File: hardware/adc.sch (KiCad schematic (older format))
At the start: 39 parts, among them U39 LP5907-3.0, U8 LTC2292

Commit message: Finished design, began routing.
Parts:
- U10: renamed from U39; value LP5907-3.0 -> LP5907MFX-3.0
- renumbered C25 to C100, C225 to C101, C248 to C75, C31 to C76, C249 to C77, C163 to C78, C164 to C79, C165 to C80, C166 to C81, C167 to C82, C168 to C83, C222 to C84, C230 to C85, C231 to C86, C217 to C87, C218 to C88, C19 to C89, C20 to C90, C223 to C91, C216 to C92, C220 to C93, C22 to C94, C224 to C95, C221 to C96, C23 to C97, C24 to C98, C27 to C99, FB16 to FB5, R97 to R28, R98 to R29, R99 to R30, R100 to R31, R91 to R32, R92 to R33, R93 to R34, R20 to R35, R21 to R36, U8 to U11

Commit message: Completed clock placement and routing.
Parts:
- removed C86: 100n, Capacitor_SMD:C_0402_1005Metric, symbol Device:C
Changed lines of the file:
@@
 	0    1    1    0
 $EndComp
-Wire Wire Line
-	4900 1050 5050 1050
-$Comp
-L Device:C C86
-U 1 1 5D84B592
-P 5050 1250
-F 0 "C86" H 5165 1296 50  0000 L CNN
-F 1 "100n" H 5165 1205 50  0000 L CNN
-F 2 "Capacitor_SMD:C_0402_1005Metric" H 5088 1100 30  0001 C CNN
-F 3 "" H 5050 1250 60  0000 C CNN
-F 4 "CL05B104KO5NNNC" H -550 50  50  0001 C CNN "MFN"
-	1    5050 1250
-	1    0    0    -1
-$EndComp
-Wire Wire Line
-	5050 1100 5050 1050
-Connection ~ 5050 1050
-Wire Wire Line
-	5050 1050 5400 1050
-$Comp
-L power:GND #PWR079
-U 1 1 5D852C8A
-P 5050 1450
-F 0 "#PWR079" H 5050 1200 50  0001 C CNN
-F 1 "GND" H 5055 1277 50  0000 C CNN
-F 2 "" H 5050 1450 50  0001 C CNN
-F 3 "" H 5050 1450 50  0001 C CNN
-	1    5050 1450
-	1    0    0    -1
-$EndComp
-Wire Wire Line
-	5050 1450 5050 1400
-$Comp
-L Device:C C85
-U 1 1 5D85A49D
-P 4450 1250
-F 0 "C85" H 4565 1296 50  0000 L CNN
-F 1 "100n" H 4565 1205 50  0000 L CNN
-F 2 "Capacitor_SMD:C_0402_1005Metric" H 4488 1100 30  0001 C CNN
-F 3 "" H 4450 1250 60  0000 C CNN
-F 4 "CL05B104KO5NNNC" H -1150 50  50  0001 C CNN "MFN"
-	1    4450 1250
-	1    0    0    -1
-$EndComp
-Wire Wire Line
-	4450 1100 4450 1050
-Connection ~ 4450 1050
-Wire Wire Line
-	4450 1050 4600 1050
-$Comp
-L power:GND #PWR078
-U 1 1 5D861E18
-P 4450 1450
-F 0 "#PWR078" H 4450 1200 50  0001 C CNN
-F 1 "GND" H 4455 1277 50  0000 C CNN
-F 2 "" H 4450 1450 50  0001 C CNN
-F 3 "" H 4450 1450 50  0001 C CNN
-	1    4450 1450
-	1    0    0    -1
-$EndComp
-Wire Wire Line
-	4450 1450 4450 1400
 Connection ~ 4000 1050
-Wire Wire Line
-	4000 1050 4450 1050
 Wire Wire Line
 	3700 1050 4000 1050
@@
 	0    1    1    0
 $EndComp
+Wire Wire Line
+	4900 1050 5400 1050
+Wire Wire Line
+	4000 1050 4450 1050
+Wire Wire Line
+	4450 1050 4600 1050
+Connection ~ 4450 1050
+Wire Wire Line
+	4450 1100 4450 1050
+Wire Wire Line
+	4450 1450 4450 1400
+$Comp
+L power:GND #PWR078
+U 1 1 5D861E18
+P 4450 1450
+F 0 "#PWR078" H 4450 1200 50  0001 C CNN
+F 1 "GND" H 4455 1277 50  0000 C CNN
+F 2 "" H 4450 1450 50  0001 C CNN
+F 3 "" H 4450 1450 50  0001 C CNN
+	1    4450 1450
+	1    0    0    -1
+$EndComp
+$Comp
+L Device:C C85
+U 1 1 5D85A49D
+P 4450 1250
+F 0 "C85" H 4565 1296 50  0000 L CNN
+F 1 "100n" H 4565 1205 50  0000 L CNN
+F 2 "Capacitor_SMD:C_0402_1005Metric" H 4488 1100 30  0001 C CNN
+F 3 "" H 4450 1250 60  0000 C CNN
+F 4 "CL05B104KO5NNNC" H -1150 50  50  0001 C CNN "MFN"
+	1    4450 1250
+	1    0    0    -1
+$EndComp
 $EndSCHEMATC

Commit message: Place/route for ft2232h.
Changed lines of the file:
@@
 F 3 "" H 5050 3650 60  0000 C CNN
 	1    5050 3650
-	1    0    0    -1
+	-1   0    0    -1
 $EndComp
 Text HLabel 8200 2650 2    60   Output ~ 0

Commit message: Better MFNs for RF DC blocking caps.
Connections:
- net AINA+: now reaches C78.2, C79.1, R28.1, U11.1 (AINA+)
- net AINB-: now reaches C82.2, C83.1, R31.1, U11.15 (AINB-)
- net AINB+: now reaches C81.2, C82.1, R29.1, U11.16 (AINB+)
- net AINA-: now reaches C79.2, C80.1, R30.1, U11.2 (AINA-)
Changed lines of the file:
@@
 	1    0    0    -1
 $EndComp
+Text Label 5550 3050 0    50   ~ 0
+AINA+
+Text Label 5550 3150 0    50   ~ 0
+AINA-
+Text Label 5550 4450 0    50   ~ 0
+AINB+
+Text Label 5550 4550 0    50   ~ 0
+AINB-
 $EndSCHEMATC

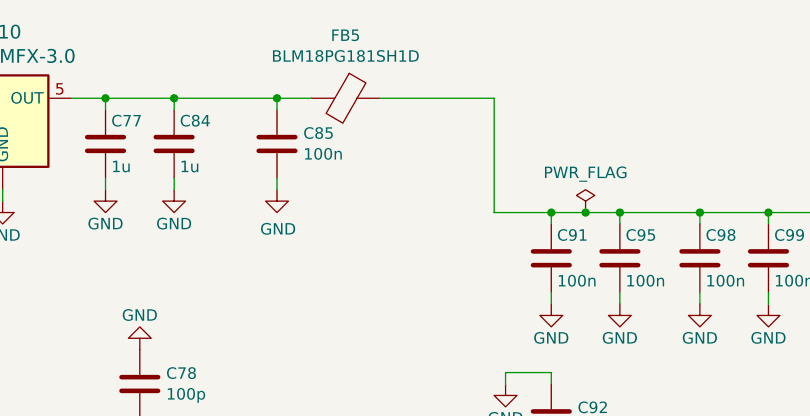
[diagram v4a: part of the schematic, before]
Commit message: Completed receivers.
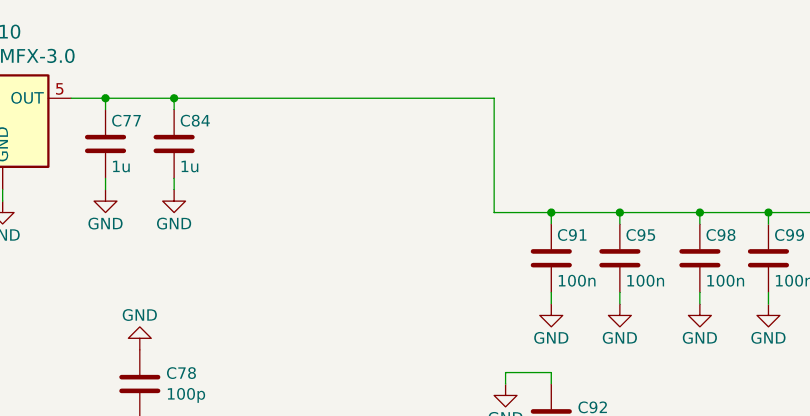
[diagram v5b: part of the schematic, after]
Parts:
- removed C85: 100n, Capacitor_SMD:C_0402_1005Metric, symbol Device:C
- removed FB5: BLM18PG181SH1D, Inductor_SMD:L_0603_1608Metric, symbol Device:Ferrite_Bead
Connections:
- net at C91.1, C95.1, C98.1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: now also C77.1, C84.1, U10.5 (OUT)
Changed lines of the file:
@@
 Wire Wire Line
 	3250 1500 3250 1450
-$Comp
-L Device:Ferrite_Bead FB?
-U 1 1 5D83CEED
-P 4750 1050
-AR Path="/5D83CEED" Ref="FB?"  Part="1"
-AR Path="/59395D6A/583E250D/5D83CEED" Ref="FB5"  Part="1"
-F 0 "FB5" V 4476 1050 50  0000 C CNN
-F 1 "BLM18PG181SH1D" V 4567 1050 50  0000 C CNN
-F 2 "Inductor_SMD:L_0603_1608Metric" H 4750 1050 60  0001 C CNN
-F 3 "https://www.murata.com/en-us/products/productdata/8796738650142/ENFA0003.pdf" H 4750 1050 60  0001 C CNN
-F 4 "BLM18PG181SH1D" H 400 -4250 50  0001 C CNN "MFN"
-	1    4750 1050
-	0    1    1    0
-$EndComp
 Connection ~ 4000 1050
 Wire Wire Line
@@
 	5650 1600 5650 1550
 Connection ~ 5650 1550
-Wire Wire Line
-	5650 1550 5800 1550
-$Comp
-L power:PWR_FLAG #FLG05
-U 1 1 5C415896
-P 5800 1550
-F 0 "#FLG05" H 5800 1625 50  0001 C CNN
-F 1 "PWR_FLAG" H 5800 1724 50  0000 C CNN
-F 2 "" H 5800 1550 50  0001 C CNN
-F 3 "~" H 5800 1550 50  0001 C CNN
-	1    5800 1550
-	1    0    0    -1
-$EndComp
-Connection ~ 5800 1550
-Wire Wire Line
-	5800 1550 5950 1550
 Wire Wire Line
 	5400 1550 5650 1550
@@
 	0    1    1    0
 $EndComp
-Wire Wire Line
-	4900 1050 5400 1050
-Wire Wire Line
-	4000 1050 4450 1050
-Wire Wire Line
-	4450 1050 4600 1050
-Connection ~ 4450 1050
-Wire Wire Line
-	4450 1100 4450 1050
-Wire Wire Line
-	4450 1450 4450 1400
-$Comp
-L power:GND #PWR078
-U 1 1 5D861E18
-P 4450 1450
-F 0 "#PWR078" H 4450 1200 50  0001 C CNN
-F 1 "GND" H 4455 1277 50  0000 C CNN
-F 2 "" H 4450 1450 50  0001 C CNN
-F 3 "" H 4450 1450 50  0001 C CNN
-	1    4450 1450
-	1    0    0    -1
-$EndComp
-$Comp
-L Device:C C85
-U 1 1 5D85A49D
-P 4450 1250
-F 0 "C85" H 4565 1296 50  0000 L CNN
-F 1 "100n" H 4565 1205 50  0000 L CNN
-F 2 "Capacitor_SMD:C_0402_1005Metric" H 4488 1100 30  0001 C CNN
-F 3 "" H 4450 1250 60  0000 C CNN
-F 4 "CL05B104KO5NNNC" H -1150 50  50  0001 C CNN "MFN"
-	1    4450 1250
-	1    0    0    -1
-$EndComp
 Text Label 5550 3050 0    50   ~ 0
 AINA+
@@
 Text Label 5550 4550 0    50   ~ 0
 AINB-
+Wire Wire Line
+	4000 1050 5400 1050
+Wire Wire Line
+	5650 1550 5950 1550
 $EndSCHEMATC

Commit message: Replaced relevant footprints for thermal via variety.
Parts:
- U11: footprint Package_DFN_QFN:QFN-64-1EP_9x9mm_P0.5mm_EP7.15x7.15mm -> Package_DFN_QFN:QFN-64-1EP_9x9mm_P0.5mm_EP7.15x7.15mm_ThermalVias
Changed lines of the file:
@@
 F 0 "U11" H 7300 4400 60  0000 C CNN
 F 1 "LTC2292" H 7300 4250 60  0000 C CNN
-F 2 "Package_DFN_QFN:QFN-64-1EP_9x9mm_P0.5mm_EP7.15x7.15mm" H 5050 6200 60  0001 C CNN
+F 2 "Package_DFN_QFN:QFN-64-1EP_9x9mm_P0.5mm_EP7.15x7.15mm_ThermalVias" H 5050 6200 60  0001 C CNN
 F 3 "" H 5050 6200 60  0001 C CNN
 F 4 "LTC2292IUP#PBF" H 1350 -100 50  0001 C CNN "MFN"

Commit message: Finish FPGA code.
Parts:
- C75: MFN CL21B106KQQNNNE -> ‎CL21B106KOQNNNE‎
- C76, C92, C93, C94: MFN CL10A225KO8NNNC -> CL10A225KA5LNNC
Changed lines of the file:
@@
 F 2 "Capacitor_SMD:C_0603_1608Metric" H 5788 3350 30  0001 C CNN
 F 3 "" H 5750 3500 60  0000 C CNN
-F 4 "CL10A225KO8NNNC" H 1600 -500 50  0001 C CNN "MFN"
+F 4 "CL10A225KA5LNNC" H 1600 -500 50  0001 C CNN "MFN"
 	1    5750 3500
 	1    0    0    -1
@@
 F 2 "Capacitor_SMD:C_0603_1608Metric" H 5688 2300 30  0001 C CNN
 F 3 "" H 5650 2450 60  0000 C CNN
-F 4 "CL10A225KO8NNNC" H -2900 -2650 50  0001 C CNN "MFN"
+F 4 "CL10A225KA5LNNC" H -2900 -2650 50  0001 C CNN "MFN"
 	1    5650 2450
 	-1   0    0    -1
@@
 F 2 "Capacitor_SMD:C_0805_2012Metric" H 2538 1100 30  0001 C CNN
 F 3 "" H 2500 1250 60  0000 C CNN
-F 4 "CL21B106KQQNNNE" H 650 -300 50  0001 C CNN "MFN"
+F 4 "‎CL21B106KOQNNNE‎" H 650 -300 50  0001 C CNN "MFN"
 	1    2500 1250
 	1    0    0    -1
@@
 F 2 "Capacitor_SMD:C_0603_1608Metric" H 5788 4750 30  0001 C CNN
 F 3 "" H 5750 4900 60  0000 C CNN
-F 4 "CL10A225KO8NNNC" H 1600 400 50  0001 C CNN "MFN"
+F 4 "CL10A225KA5LNNC" H 1600 400 50  0001 C CNN "MFN"
 	1    5750 4900
 	1    0    0    -1
@@
 F 2 "Capacitor_SMD:C_0603_1608Metric" H 3338 4100 30  0001 C CNN
 F 3 "" H 3300 4250 60  0000 C CNN
-F 4 "CL10A225KO8NNNC" H -5200 -1650 50  0001 C CNN "MFN"
+F 4 "CL10A225KA5LNNC" H -5200 -1650 50  0001 C CNN "MFN"
 	1    3300 4250
 	-1   0    0    -1
